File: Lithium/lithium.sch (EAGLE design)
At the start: 59 parts, among them J4 PJ-040X, Q1 J112, Q2 J112, Q3 ZVN4306A, Q4 ZVN4306A, Q5 ZTX694B, Q6 J112, Q7 J112, Q8 ZVN4306A, Q9 ZVN4306A

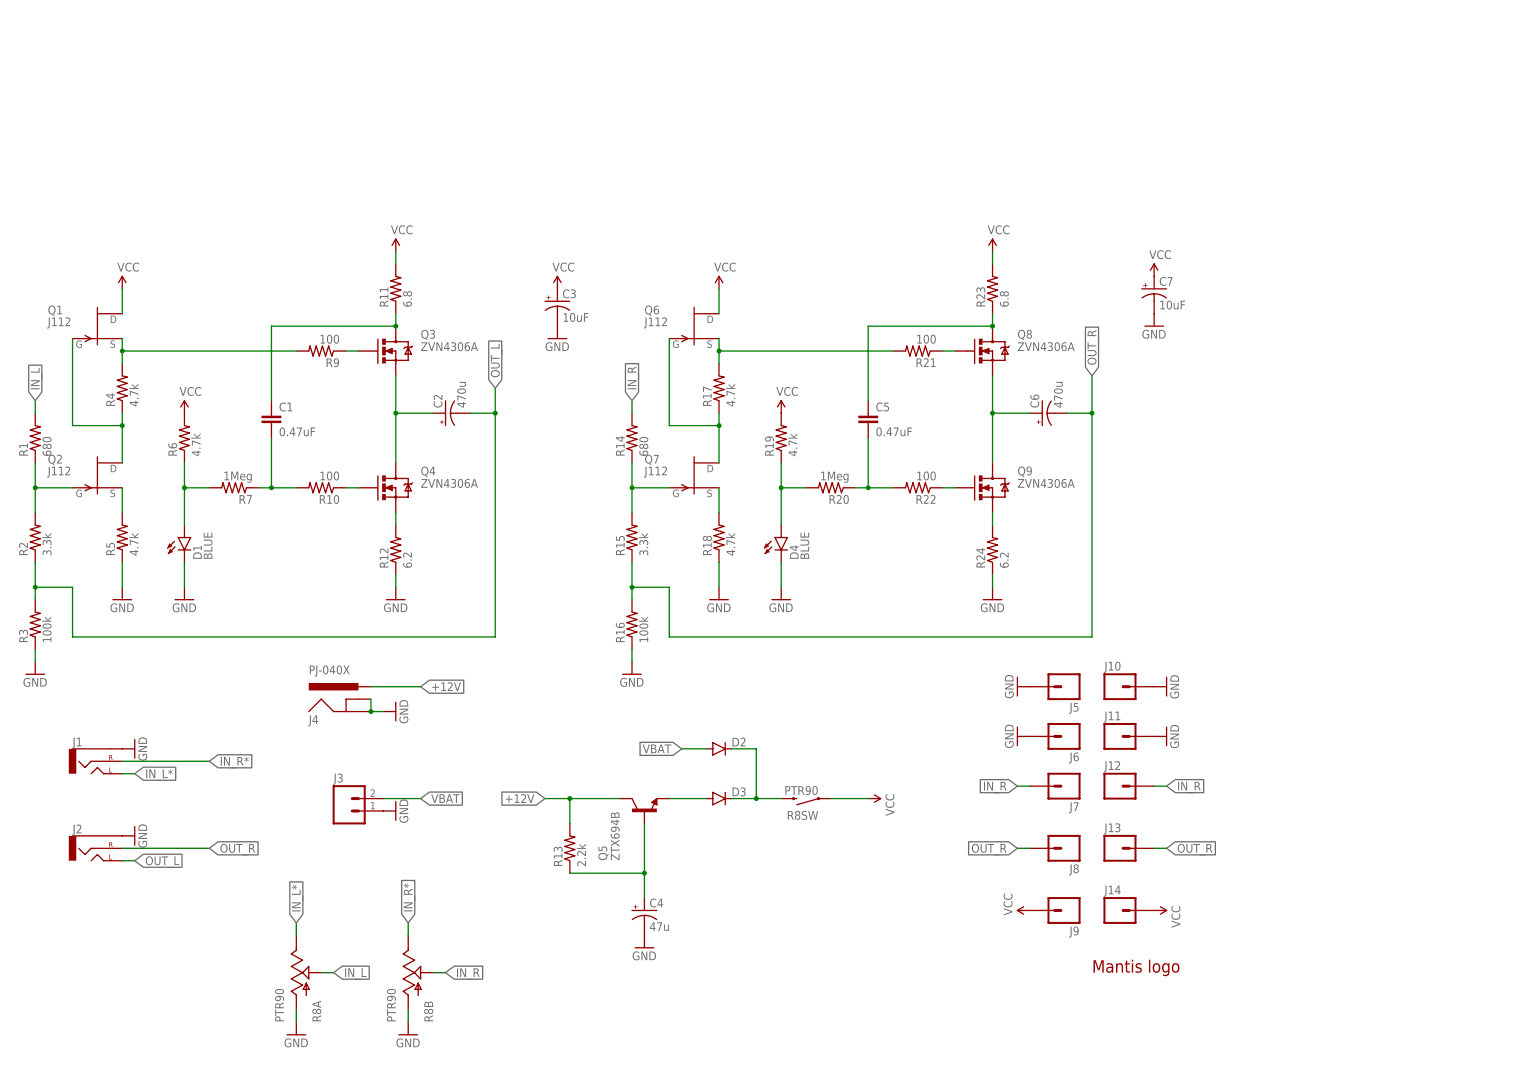
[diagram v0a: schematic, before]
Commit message: Li-ion powered version WIP
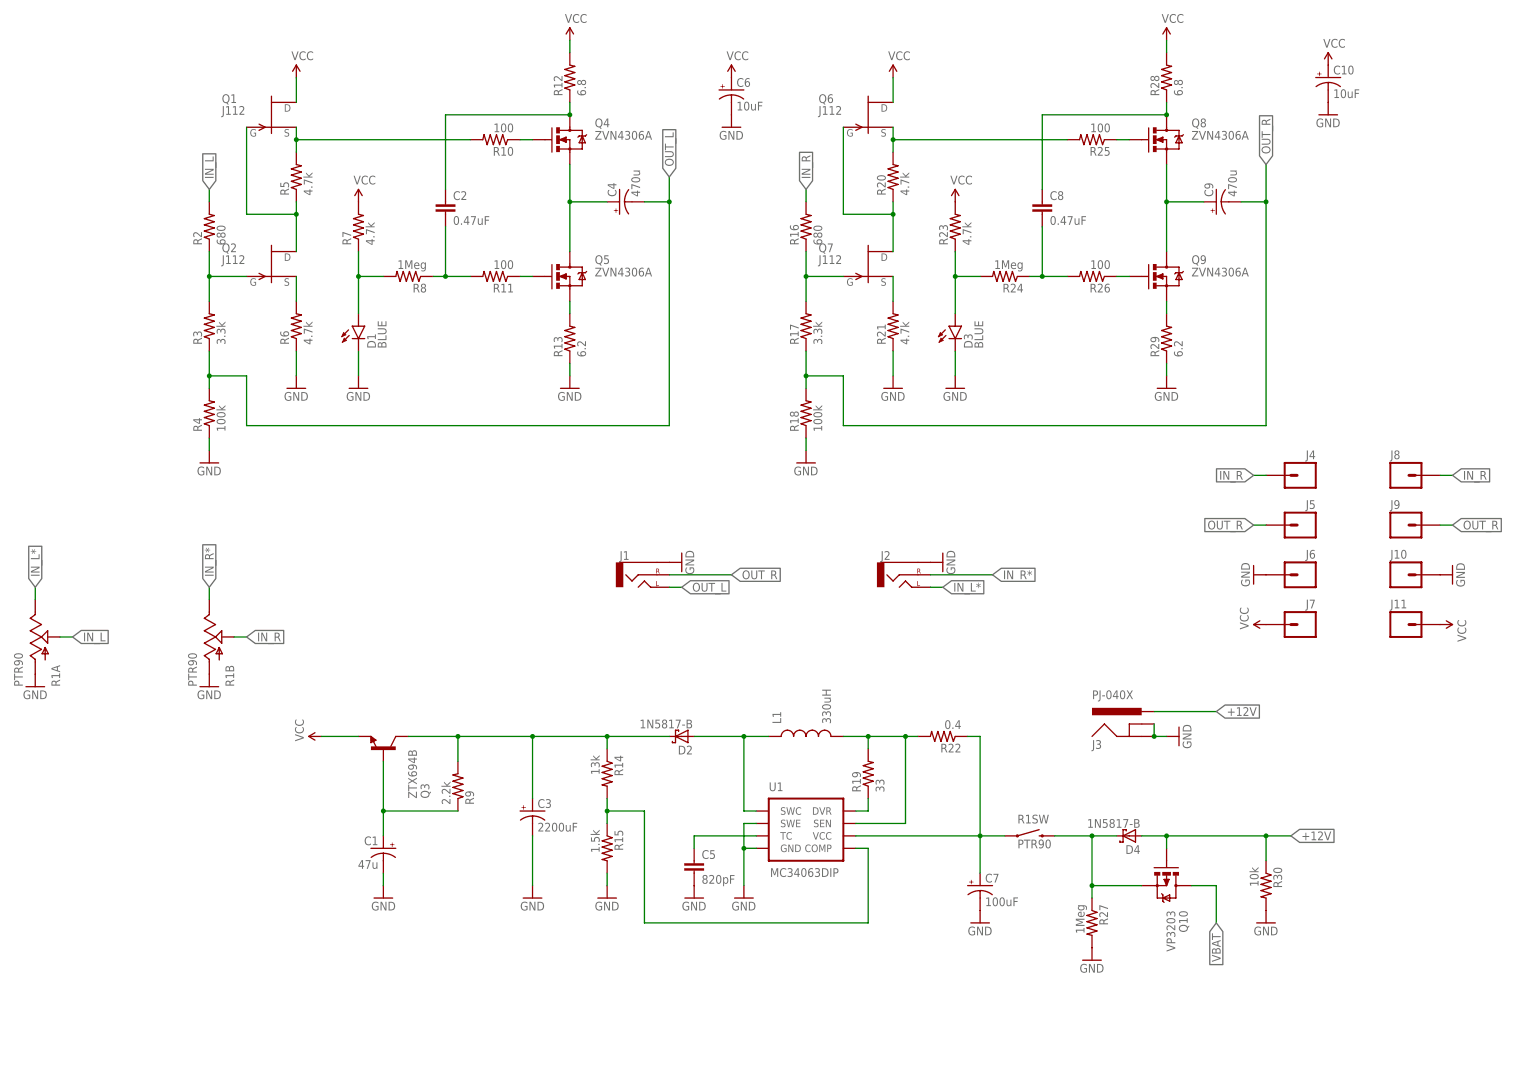
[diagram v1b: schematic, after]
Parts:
- removed J12, J13, J14: (no value), SparkFun-Connectors:M01PTH
- removed LOGO1: LOGO-MANTIS, my:LOGO-MANTIS
- added C10: 10uF, my-cap:CAP_POLPTH1-SM
- added C8: 0.47uF, capacitor-wima:C5/3.5
- added C9: 470u, my-cap:CAP_POLPTH8MM
- added L1: 330uH, SparkFun-Passives:INDUCTORRLB0912
- added Q10: VP3203, my-tran:VP3203
- added R25, R26: 100, my-res:RESISTORPTH-1/4W-SM
- added R27: 1Meg, my-res:RESISTORPTH-1/4W-SM
- added R28: 6.8, my-res:RESISTORPTH-1/4W-SM
- added R29: 6.2, my-res:RESISTORPTH-1/4W-SM
- added R30: 10k, my-res:RESISTORPTH-1/4W-SM
- added U1: MC34063DIP, SparkFun-PowerIC:MC34063DIP
- C1: value 0.47uF -> 47u; device capacitor-wima:C5/3.5 -> my-cap:CAP_POLPTH1-SM
- C2: value 470u -> 0.47uF; device my-cap:CAP_POLPTH8MM -> capacitor-wima:C5/3.5
- C3: value 10uF -> 2200uF; device my-cap:CAP_POLPTH1-SM -> SparkFun-Capacitors:CAP_POLPTH4
- C4: value 47u -> 470u; device my-cap:CAP_POLPTH1-SM -> my-cap:CAP_POLPTH8MM
- C5: value 0.47uF -> 820pF; device capacitor-wima:C5/3.5 -> SparkFun-Capacitors:CAPPTH
- C6: value 470u -> 10uF; device my-cap:CAP_POLPTH8MM -> my-cap:CAP_POLPTH1-SM
- C7: value 10uF -> 100uF; device my-cap:CAP_POLPTH1-SM -> SparkFun-Capacitors:CAP_POLPTH1
- D2: value (none) -> 1N5817-B; device SparkFun-DiscreteSemi:DIODEPTH -> diode:1N5817-B
- D3: value (none) -> BLUE; device SparkFun-DiscreteSemi:DIODEPTH -> my:LED3MM-SM
- D4: value BLUE -> 1N5817-B; device my:LED3MM-SM -> diode:1N5817-B
- J3: value (none) -> PJ-040X; device SparkFun-Connectors:M02PTH -> my-conn:PJ-040X
- J4: value PJ-040X -> (none); device my-conn:PJ-040X -> SparkFun-Connectors:M01PTH
- Q3: value ZVN4306A -> ZTX694B; device my-tran:ZVN4306A -> my-tran:ZTX694B
- Q5: value ZTX694B -> ZVN4306A; device my-tran:ZTX694B -> my-tran:ZVN4306A
- R1: value 680 -> PTR90; device my-res:RESISTORPTH-1/4W-SM -> my:PTR90
- R11: value 6.8 -> 100
- R12: value 6.2 -> 6.8
- R13: value 2.2k -> 6.2
- R14: value 680 -> 13k
- R15: value 3.3k -> 1.5k
- R16: value 100k -> 680
- R17: value 4.7k -> 3.3k
- R18, R4: value 4.7k -> 100k
- R19: value 4.7k -> 33
- R2: value 3.3k -> 680
- R20, R7: value 1Meg -> 4.7k
- R21: value 100 -> 4.7k
- R22: value 100 -> 0.4
- R23: value 6.8 -> 4.7k
- R24: value 6.2 -> 1Meg
- R3: value 100k -> 3.3k
- R8: value PTR90 -> 1Meg; device my:PTR90 -> my-res:RESISTORPTH-1/4W-SM
- R9: value 100 -> 2.2k
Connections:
- removed net N$5 (its old number): Q3.G, R9.1
- removed net VCC*: D2.C, D3.C, R8SW.2
- new net N$18: R19.1, U1.DVR
- new net N$25: D2.A, L1.1, U1.SWC
- new net N$26: L1.2, R19.2, R22.2, U1.SEN
- new net N$28: R14.2, R15.1, U1.COMP
- new net N$29: D4.C, Q10.S, R1SW.2, R27.1
- new net N$8: Q5.G, R11.1
- new net N$9: C5.1, U1.TC
- new net VSMPS: C3.+, D2.C, Q3.C, R14.1, R9.2
- net +12V: now also D4.A, J3.PWR, Q10.G, R30.1; no longer J4.PWR, Q5.C, R13.2
- net GND: now also C1.-, C10.-, C5.2, C6.-, D3.C, J3.GND, J3.GNDBREAK, R13.1, R15.2, R1A.A, R1B.A, R21.1, R27.2, R29.1, R30.2, R4.1, R6.1, U1.GND, U1.SWE; no longer C4.-, D4.C, J11.1, J3.1, J4.GND, J4.GNDBREAK, J5.1, R12.1, R16.1, R24.1, R3.1, R5.1, R8A.A, R8B.A
- net IN_L: now also R1A.S, R2.2; no longer R1.2, R8A.S
- net IN_L*: now also J2.LEFT, R1A.E; no longer J1.LEFT, R8A.E
- net IN_R: now also J4.1, J8.1, R16.2, R1B.S; no longer J12.1, J7.1, R14.2, R8B.S
- net IN_R*: now also J2.RIGHT, R1B.E; no longer J1.RIGHT, R8B.E
- net N$1: now also R10.2, R5.2; no longer R4.2, R9.2
- net N$10: now also Q5.S, R13.2; no longer Q4.S, R12.2
- net N$11: now also C2.1, Q4.D, R12.1; no longer C1.1, Q3.D, R11.1
- net N$12: now also R21.2; no longer R18.2
- net N$13: now also C2.2, R11.2, R8.1; no longer C1.2, R10.2, R7.1
- net N$14: now also R7.1, R8.2; no longer R6.1, R7.2
- net N$15: now also R16.1, R17.2; no longer R14.1, R15.2
- net N$16: now also R25.1; no longer R21.1
- net N$17: now also R26.1; no longer R22.1
- net N$19: now also R29.2; no longer R24.2
- net N$2: now also R5.1; no longer R4.1
- net N$20: now also C8.1, R28.1; no longer C5.1, R23.1
- net N$21: now also C8.2, R24.1, R26.2; no longer C5.2, R20.1, R22.2
- net N$22: now also D3.A, R23.1, R24.2; no longer D4.A, R19.1, R20.2
- net N$23: now also C7.+, R1SW.1, R22.1, U1.VCC; no longer D3.A, Q5.E
- net N$24: now also C1.+, Q3.B, R9.1; no longer C4.+, Q5.B, R13.1
- net N$3: now also R6.2; no longer R5.2
- net N$4: now also R20.2, R25.2; no longer R17.2, R21.2
- net N$6: now also R2.1, R3.2; no longer R1.1, R2.2
- net N$7: now also R20.1; no longer R17.1
- net OUT_L: now also C4.-, J1.LEFT, R3.1, R4.2; no longer C2.-, J2.LEFT, R2.1, R3.2
- net OUT_L*: now also C4.+, Q4.S, Q5.D; no longer C2.+, Q3.S, Q4.D
- net OUT_R: now also C9.-, J1.RIGHT, J5.1, J9.1, R17.1, R18.2; no longer C6.-, J13.1, J2.RIGHT, J8.1, R15.1, R16.2
- net OUT_R*: now also C9.+; no longer C6.+
- net VBAT: now also Q10.D; no longer D2.A, J3.2
- net VCC: now also C10.+, C6.+, J11.1, J7.1, Q3.E, R12.2, R28.2, R7.2; no longer C3.+, C7.+, J14.1, J9.1, R11.2, R19.2, R6.2, R8SW.1
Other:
- moved on the sheet: C3, C4, C5, C6, C7, D1, J1, J10, J11, J2, J3, J5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

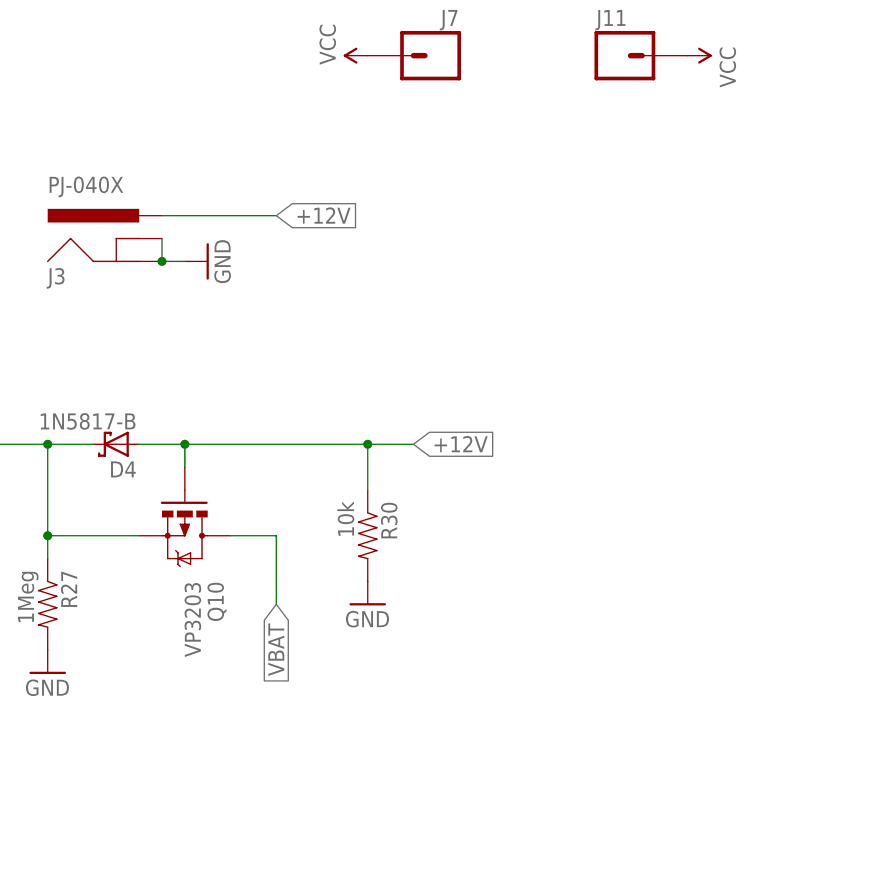
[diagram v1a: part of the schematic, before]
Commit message: Stamp holes removed
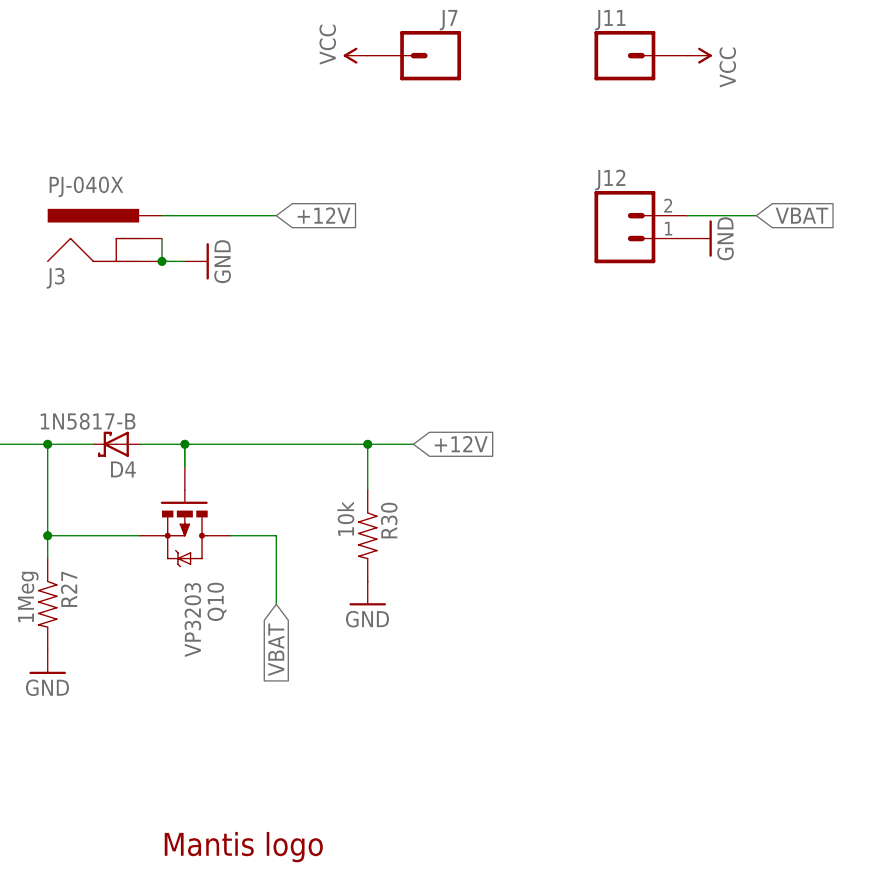
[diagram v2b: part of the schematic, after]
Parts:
- added J12: (no value), SparkFun-Connectors:M02PTH
- added LOGO1: LOGO-MANTIS, my:LOGO-MANTIS
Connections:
- net GND: now also J12.1
- net VBAT: now also J12.2
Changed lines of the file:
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@@
 <part name="SUPPLY11" library="SparkFun-Aesthetics" deviceset="VCC" device=""/>
 <part name="SUPPLY9" library="SparkFun-Aesthetics" deviceset="VCC" device=""/>
+<part name="LOGO1" library="my" deviceset="LOGO-MANTIS" device=""/>
+<part name="J12" library="SparkFun-Connectors" deviceset="M02" device="PTH"/>
+<part name="GND26" library="SparkFun-Aesthetics" deviceset="GND" device=""/>
 </parts>
 <sheets>
@@
 <instance part="SUPPLY11" gate="G$1" x="320.04" y="96.52" rot="R270"/>
 <instance part="SUPPLY9" gate="G$1" x="284.48" y="96.52" rot="R90"/>
+<instance part="LOGO1" gate="G$1" x="271.78" y="7.62"/>
+<instance part="J12" gate="G$1" x="312.42" y="76.2"/>
+<instance part="GND26" gate="1" x="322.58" y="76.2" rot="R90"/>
 </instances>
 <busses>
@@
 <pinref part="J10" gate="G$1" pin="1"/>
 <pinref part="GND25" gate="1" pin="GND"/>
+</segment>
+<segment>
+<pinref part="J12" gate="G$1" pin="1"/>
+<pinref part="GND26" gate="1" pin="GND"/>
 </segment>
 </net>
@@
 <label x="274.32" y="35.56" size="1.778" layer="95" rot="R270" xref="yes"/>
 </segment>
-</net>
+<segment>
+<pinref part="J12" gate="G$1" pin="2"/>
+<wire x1="320.04" y1="78.74" x2="327.66" y2="78.74" width="0.1524" layer="91"/>
+<label x="327.66" y="78.74" size="1.778" layer="95" xref="yes"/>
+</segment>
+</net>
